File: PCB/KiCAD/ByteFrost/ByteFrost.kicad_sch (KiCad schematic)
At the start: 6 parts, among them U1 74HC374, U2 74HC374, U3 74HC374, U4 74HC374, U5 74LS139, U6 74HC02

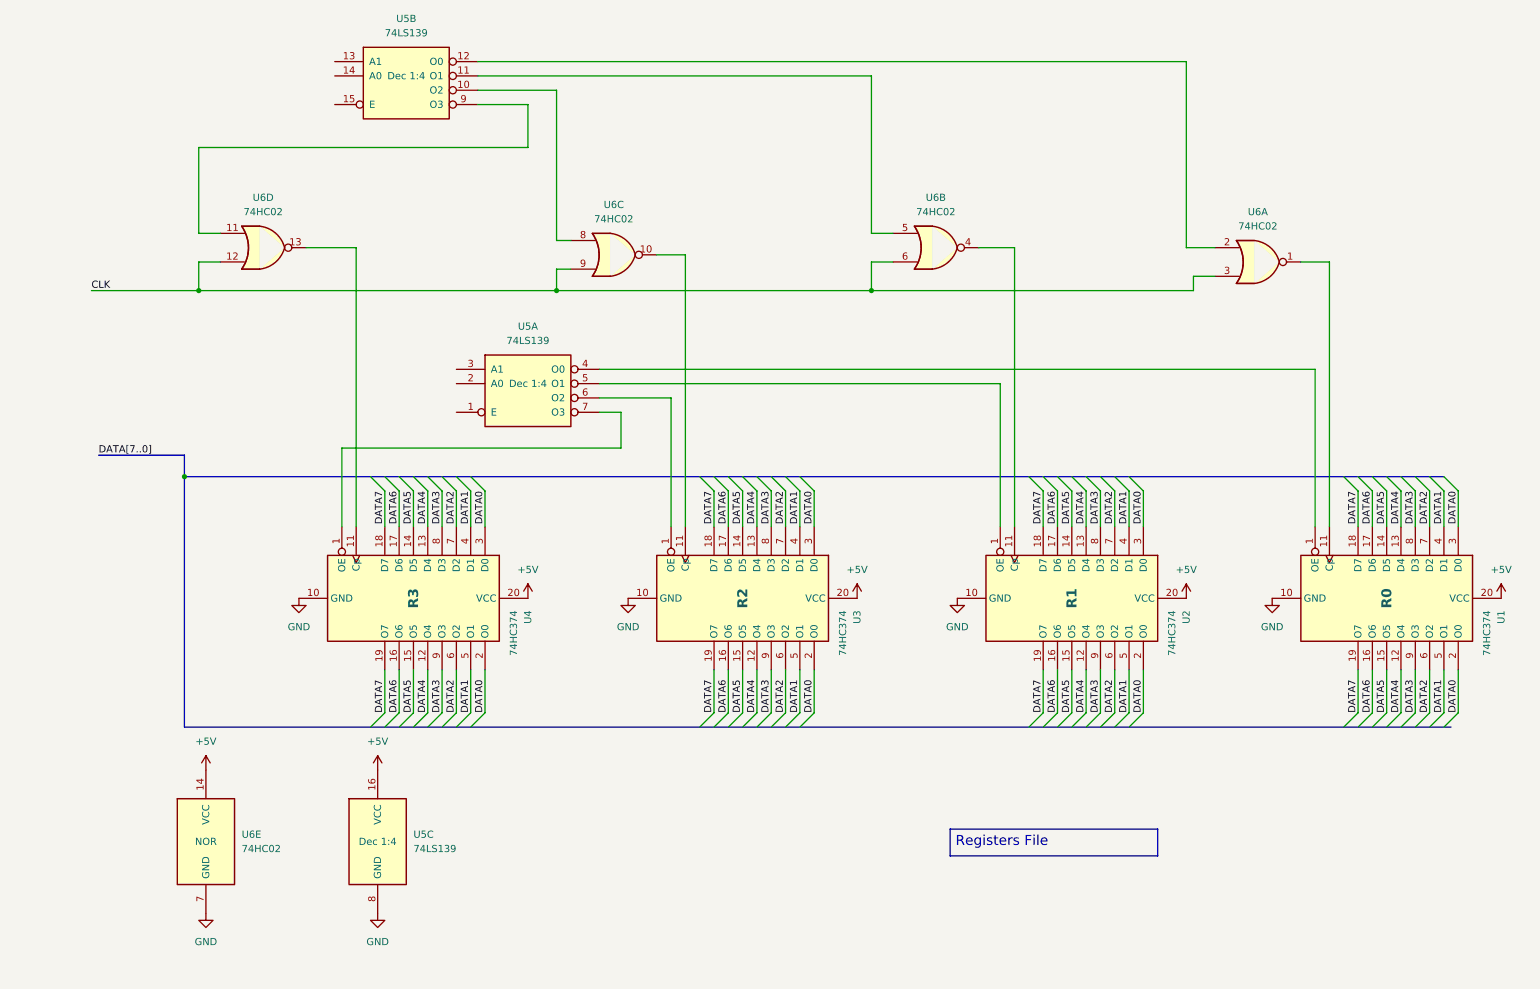
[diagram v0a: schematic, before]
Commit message: BootROM run BIST and loads SD Card
Now need to fix the code in the SD to run Shell
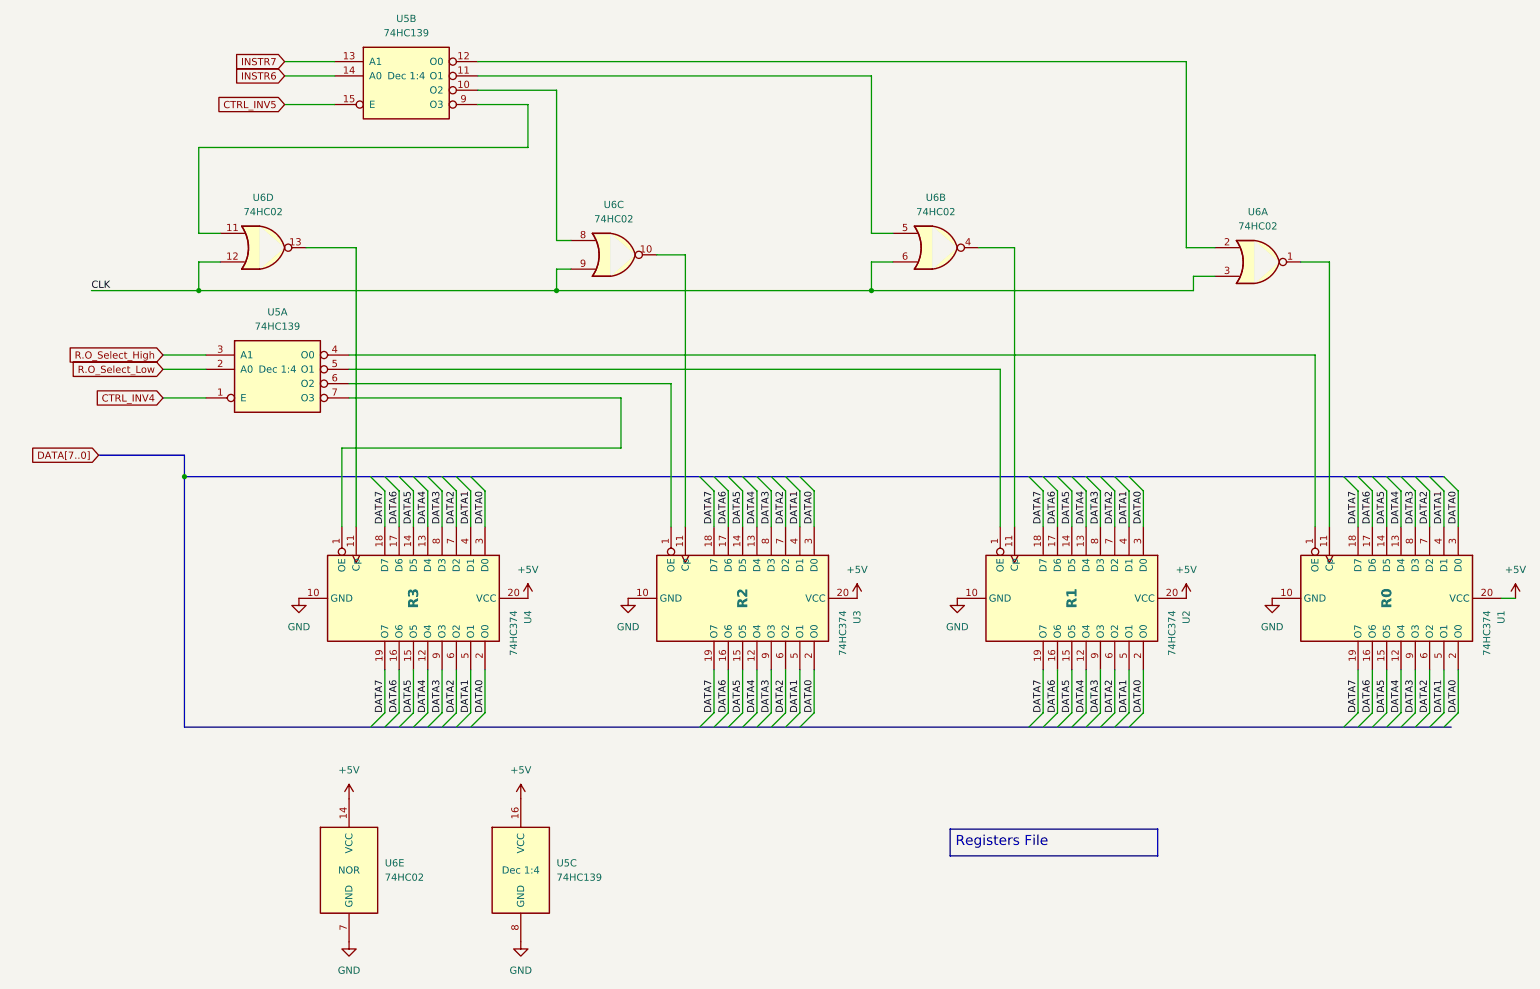
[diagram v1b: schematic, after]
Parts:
- U5: value 74LS139 -> 74HC139
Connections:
- net CTRL_INV4: now reaches U5.1 (E)
- net R.O_Select_Low: now reaches U5.2 (A0)
- net R.O_Select_High: now reaches U5.3 (A1)
- net INSTR7: now reaches U5.13 (A1)
- net INSTR6: now reaches U5.14 (A0)
- net CTRL_INV5: now reaches U5.15 (E)
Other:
- moved on the sheet: U5A, U5C, U6E

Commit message: Finish KiCAD Clock and Reset
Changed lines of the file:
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@@
+	)
+	(junction
+		(at 163.83 72.39)
+		(diameter 0)
+		(color 0 0 0 0)
 	)
 	(junction
@@
 	)
 	(junction
-		(at 163.83 72.39)
-		(diameter 0)
-		(color 0 0 0 0)
-	)
-	(junction
 		(at 41.91 105.41)
 		(diameter 0)
@@
 	(wire
 		(pts
-			(xy 25.4 72.39) (xy 44.45 72.39)
-		)
-		(stroke
-			(width 0)
-			(type default)
-		)
-	)
-	(wire
-		(pts
 			(xy 38.1 86.36) (xy 45.72 86.36)
 		)
@@
 		(pts
 			(xy 95.25 107.95) (xy 95.25 114.3)
+		)
+		(stroke
+			(width 0)
+			(type default)
+		)
+	)
+	(wire
+		(pts
+			(xy 27.94 72.39) (xy 44.45 72.39)
 		)
 		(stroke
@@
 			)
 			(justify right bottom)
-		)
-	)
-	(label "CLK"
-		(at 25.4 72.39 0)
-		(effects
-			(font
-				(size 1.27 1.27)
-			)
-			(justify left bottom)
 		)
 	)
@@
 			(show_name no)
 			(do_not_autoplace no)
+			(effects
+				(font
+					(size 1.27 1.27)
+				)
+				(justify right)
+			)
+		)
+	)
+	(global_label "CLK"
+		(shape input)
+		(at 27.94 72.39 180)
+		(fields_autoplaced yes)
+		(effects
+			(font
+				(size 1.27 1.27)
+			)
+			(justify right)
+		)
+		(property "Intersheetrefs" "${INTERSHEET_REFS}"
+			(at 21.3867 72.39 0)
+			(show_name no)
+			(do_not_autoplace no)
